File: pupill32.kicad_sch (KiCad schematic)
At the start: 53 parts, among them J1 HeaderR, J2 HeaderL, J3 USB_PINS, J4 SWD_HEADER, SW1 RST_BTN, SW2 BOOT_BTN, U1 SRV05-4, U2 PY32F030F18P6, U3 CH340N, U4 AMS1117-3.3, Y1 32.768 kHz, Y2 12M

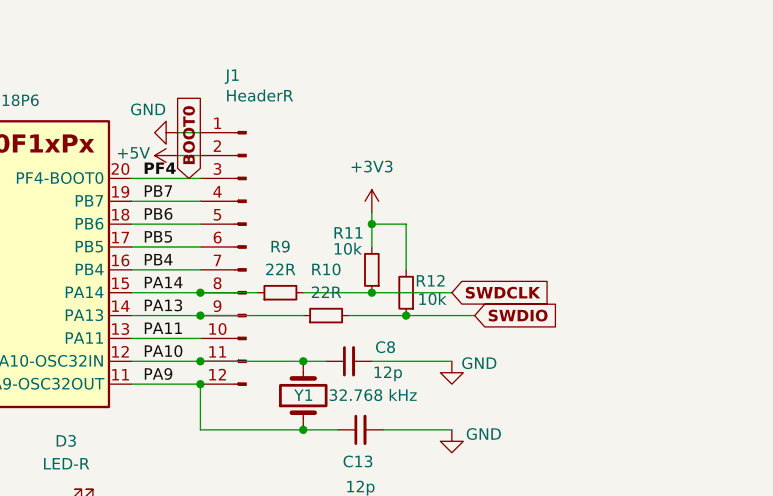
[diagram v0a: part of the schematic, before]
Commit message: SWCLK pulled down (corrected)
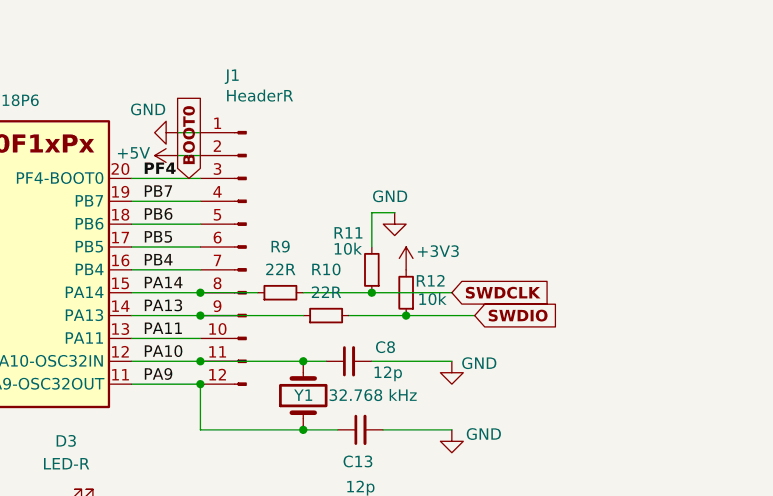
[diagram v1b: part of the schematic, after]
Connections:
- net +3V3: no longer R11.2
- net GND: now also R11.2
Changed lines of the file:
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@@
 	)
 	(junction
-		(at 264.16 41.91)
-		(diameter 0)
-		(color 0 0 0 0)
-	)
-	(junction
 		(at 245.11 52.07)
 		(diameter 0)
@@
 	(wire
 		(pts
-			(xy 267.97 41.91) (xy 264.16 41.91)
-		)
-		(stroke
-			(width 0)
-			(type default)
-		)
-	)
-	(wire
-		(pts
 			(xy 105.41 160.02) (xy 110.49 160.02)
 		)
@@
 	(wire
 		(pts
+			(xy 264.16 40.64) (xy 266.7 40.64)
+		)
+		(stroke
+			(width 0)
+			(type default)
+		)
+	)
+	(wire
+		(pts
 			(xy 50.8 116.84) (xy 67.31 116.84)
 		)
@@
 	(wire
 		(pts
-			(xy 264.16 40.64) (xy 264.16 41.91)
+			(xy 264.16 40.64) (xy 264.16 44.45)
 		)
 		(stroke
@@
 	(wire
 		(pts
-			(xy 267.97 46.99) (xy 267.97 41.91)
-		)
-		(stroke
-			(width 0)
-			(type default)
-		)
-	)
-	(wire
-		(pts
 			(xy 237.49 39.37) (xy 245.11 39.37)
 		)
@@
 	(wire
 		(pts
-			(xy 264.16 41.91) (xy 264.16 44.45)
-		)
-		(stroke
-			(width 0)
-			(type default)
-		)
-	)
-	(wire
-		(pts
 			(xy 67.31 116.84) (xy 67.31 120.65)
 		)
@@
 	(symbol
 		(lib_id "power:+3V3")
-		(at 264.16 40.64 0)
+		(at 267.97 46.99 0)
 		(unit 1)
 		(exclude_from_sim no)
@@
 		(on_board yes)
 		(dnp no)
-		(fields_autoplaced yes)
 		(property "Reference" "#PWR048"
-			(at 264.16 44.45 0)
+			(at 267.97 50.8 0)
 			(effects
 				(font
@@
 		)
 		(property "Value" "+3V3"
-			(at 264.16 35.56 0)
+			(at 271.526 44.958 0)
 			(effects
 				(font
@@
 		)
 		(property "Footprint" ""
-			(at 264.16 40.64 0)
+			(at 267.97 46.99 0)
 			(effects
 				(font
@@
 		)
 		(property "Datasheet" ""
-			(at 264.16 40.64 0)
+			(at 267.97 46.99 0)
 			(effects
 				(font
@@
 		)
 		(property "Description" ""
-			(at 264.16 40.64 0)
+			(at 267.97 46.99 0)
 			(effects
 				(font
@@
 					(unit 1)
 				)
+			)
+		)
+	)
+	(symbol
+		(lib_id "power:GND")
+		(at 266.7 40.64 0)
+		(unit 1)
+		(exclude_from_sim no)
+		(in_bom yes)
+		(on_board yes)
+		(dnp no)
+		(property "Reference" "#PWR049"
+			(at 266.7 46.99 0)
+			(effects
+				(font
+					(size 1.27 1.27)
+				)
+				(hide yes)
+			)
+		)
+		(property "Value" "GND"
+			(at 266.192 38.862 0)
+			(effects
+				(font
+					(size 1.27 1.27)
+				)
+			)
+		)
+		(property "Footprint" ""
+			(at 266.7 40.64 0)
+			(effects
+				(font
+					(size 1.27 1.27)
+				)
+				(hide yes)
+			)
+		)
+		(property "Datasheet" ""
+			(at 266.7 40.64 0)
+			(effects
+				(font
+					(size 1.27 1.27)
+				)
+				(hide yes)
+			)
+		)
+		(property "Description" ""
+			(at 266.7 40.64 0)
+			(effects
+				(font
+					(size 1.27 1.27)
+				)
+				(hide yes)
+			)
+		)
+		(pin "1"
+		)
+		(instances
+			(project "pupill32"
+				(path "/0471bd21-091d-469f-a793-0e3efa813f7b"
+					(reference "#PWR049")
+					(unit 1)
+				)
